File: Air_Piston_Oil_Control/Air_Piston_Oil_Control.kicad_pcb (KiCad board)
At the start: 2 copper layers, 54.6 x 62.2 mm, 53 parts, among them J1 Conn_01x20_Pin, J2 Conn_02x06_Odd_Even, Q1 CPC1966YX6, Q2 NTR4003NT3G, U1 STM32G431RBT6, U2 AMS1117-3.3, U4 LTL-30EHJH96, U5 MAX6817EUT_T, U6 CPC1966YX6, U7 CPC1966YX6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

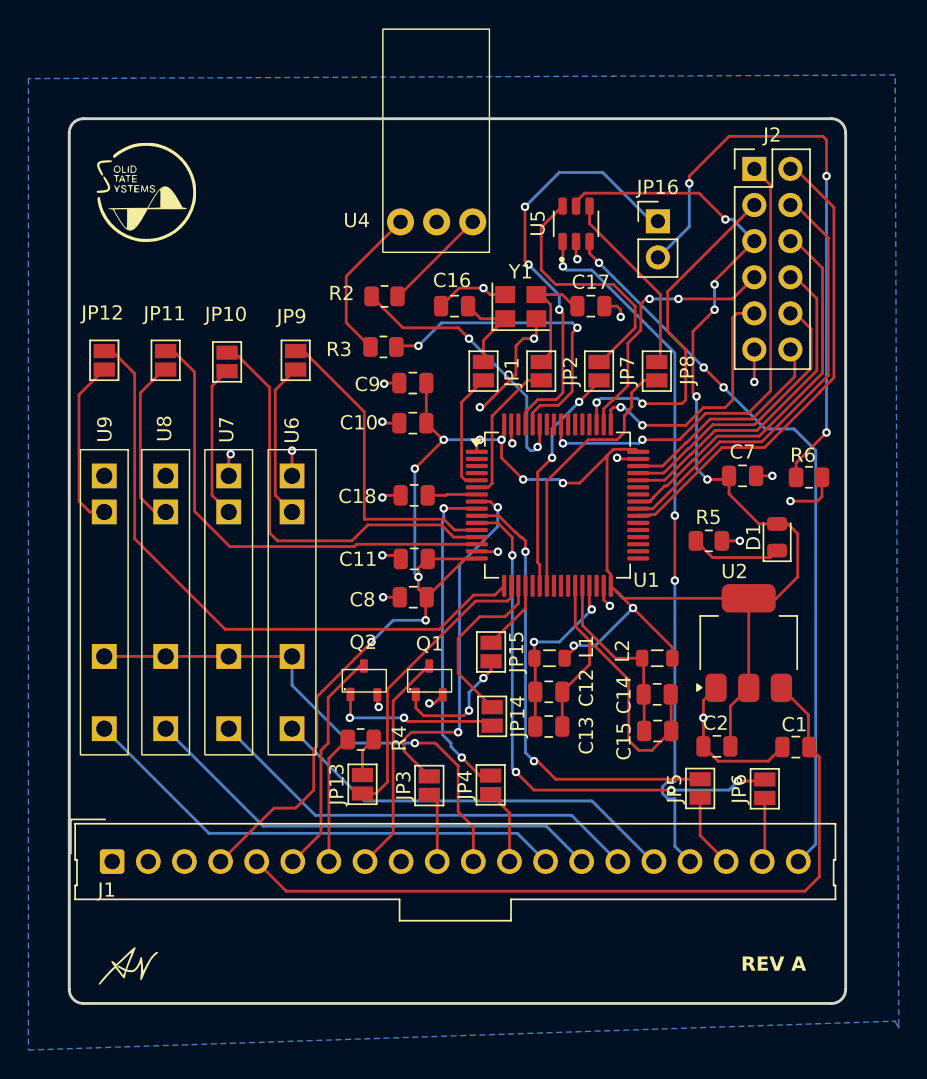
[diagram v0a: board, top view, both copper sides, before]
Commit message: Ver B manufacturing, removed solder pads
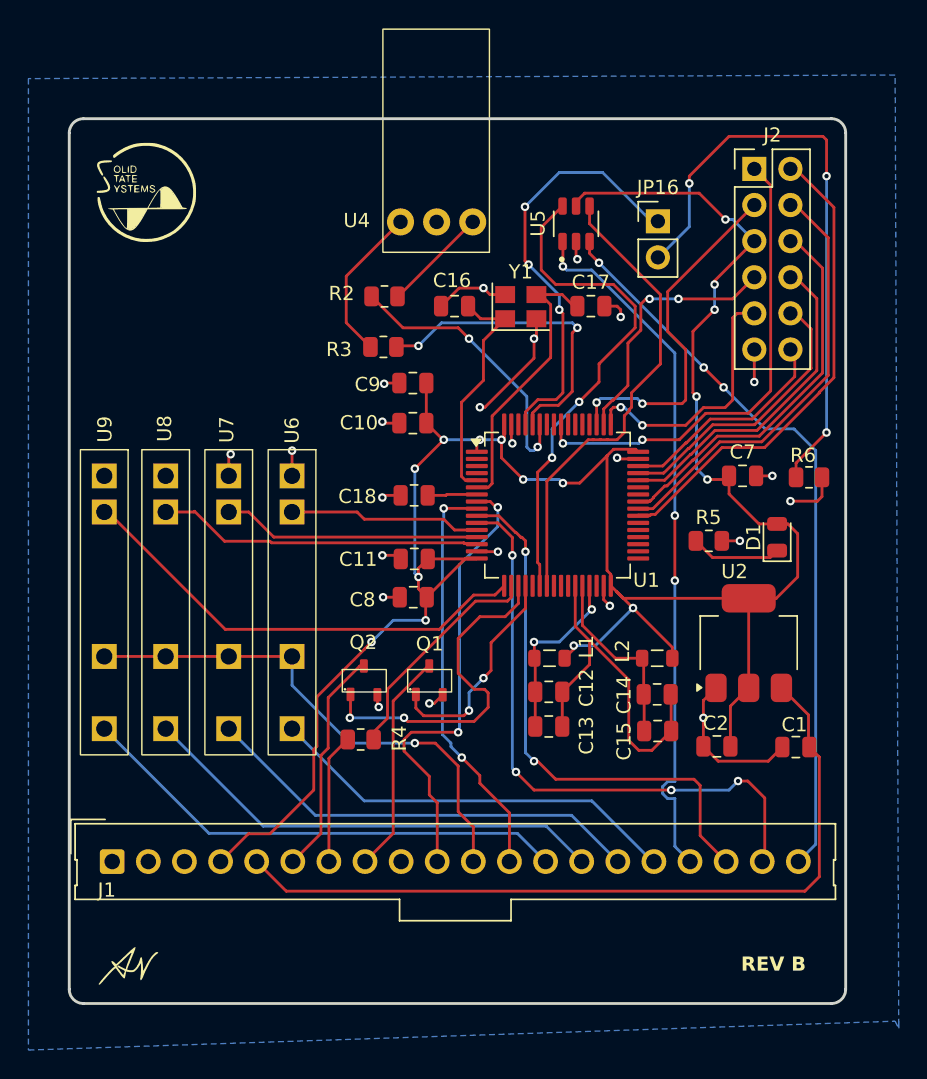
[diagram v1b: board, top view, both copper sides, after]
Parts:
- removed JP1, JP10, JP11, JP12, JP13, JP14, JP15, JP2, JP3, JP4, JP5, JP6, JP7, JP8, JP9: SolderJumper_2_Open, Jumper:SolderJumper-2_P1.3mm_Open_Pad1.0x1.5mm
- C10, C12, C14, C18, C7, C8, C9: value 100n -> 100nF
- C11: value 4.7u -> 4.7uF
- C13, C15: value 1u -> 1uF
- C16, C17: value 6.8p -> 6.8pF
- Q1: value CPC1966YX6 -> NTR4003NT3G
- R2, R3, R4, R5: value 1K -> 1k
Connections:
- C16 pad 1: Net-(JP1-B) -> Net-(U1-PF0)
- C17 pad 1: Net-(JP2-A) -> Net-(U1-PF1)
- U1 pad 10: Net-(JP5-B) -> TEMP_SENS1
- U1 pad 11: Net-(JP6-B) -> TEMP_SENS2
- U1 pad 12: Net-(JP9-A) -> SIG_OILER
- U1 pad 13: Net-(JP10-A) -> SIG_SOLENOID2
- U1 pad 14: Net-(JP11-A) -> SIG_SOLENOID1
- U1 pad 17: Net-(JP12-A) -> SIG_CLAMP
- U1 pad 18: Net-(JP13-A) -> MACHINE_LED
- U1 pad 19: Net-(JP14-A) -> MAG_MOSFET
- U1 pad 20: Net-(JP15-A) -> DEMAG_MOSFET
- U1 pad 22: Net-(JP7-B) -> MAG_IN
- U1 pad 23: Net-(JP8-B) -> DEMAG_IN
- U1 pad 5: Net-(JP1-A) -> Net-(U1-PF0)
- U1 pad 6: Net-(JP2-B) -> Net-(U1-PF1)
- U1 pad 8: Net-(JP3-B) -> SPRAY_TIME/S5
- U1 pad 9: Net-(JP4-B) -> AC1/OVERHEAT_LED
- Y1 pad 1: Net-(JP1-B) -> Net-(U1-PF0)
- Y1 pad 3: Net-(JP2-A) -> Net-(U1-PF1)
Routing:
- net Net-(JP12-A): track 44.3 -> 0.00 mm
- net TEMP_SENS2: track 4.54 -> 42.9 mm, vias 0 -> 4
- net Net-(JP6-B): track 37.9 -> 0.00 mm, vias 4 -> 0
- net Net-(JP11-A): track 33.4 -> 0.00 mm
- net TEMP_SENS1: track 5.25 -> 38.4 mm, vias 0 -> 2
- net Net-(JP5-B): track 32.1 -> 0.00 mm, vias 2 -> 0
- net Net-(JP10-A): track 29.9 -> 0.00 mm
- net SPRAY_TIME/S5: track 4.93 -> 32.2 mm, vias 0 -> 2
- net Net-(JP3-B): track 26.0 -> 0.00 mm, vias 2 -> 0
- net AC1/OVERHEAT_LED: track 5.29 -> 29.2 mm, vias 0 -> 2
- net Net-(JP4-B): track 23.0 -> 0.00 mm, vias 2 -> 0
- net Net-(JP9-A): track 22.4 -> 0.00 mm
- net Net-(JP13-A): track 20.8 -> 0.00 mm
- net SIG_CLAMP: track 12.1 -> 32.8 mm
- net DEMAG_IN: track 13.1 -> 33.3 mm
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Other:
- board text added: "REV B"
- board text removed: "REV A"
